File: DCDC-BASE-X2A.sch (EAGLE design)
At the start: 7 parts

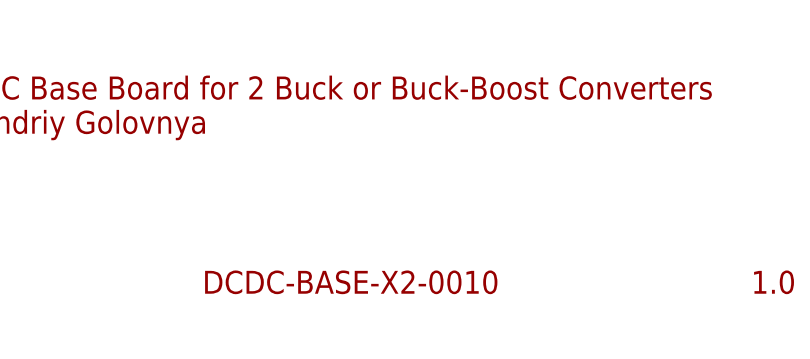
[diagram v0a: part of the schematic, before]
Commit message: Renamed X2 board to X2A. Generated CAM files. Generated PNG preview. Generated PDF schematics. Updated descriptions.
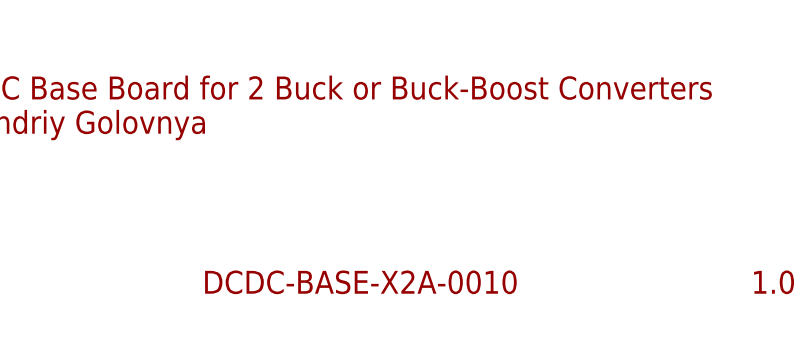
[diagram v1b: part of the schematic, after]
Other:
- note added: "DCDC-BASE-X2A-0010"
- note removed: "DCDC-BASE-X2-0010"
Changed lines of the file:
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@@
 <plain>
 <text x="256.54" y="7.62" size="2.54" layer="94">1.0</text>
-<text x="195.58" y="7.62" size="2.54" layer="94">DCDC-BASE-X2-0010</text>
+<text x="195.58" y="7.62" size="2.54" layer="94">DCDC-BASE-X2A-0010</text>
 <text x="165.1" y="25.4" size="2.54" layer="94">DC/DC Base Board for 2 Buck or Buck-Boost Converters
 (c) Andriy Golovnya</text>
